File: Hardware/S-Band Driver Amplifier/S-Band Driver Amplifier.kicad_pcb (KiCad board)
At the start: 2 copper layers, 31.8 x 25.4 mm, 15 parts, among them J1 Conn_Coaxial, J2 Conn_Coaxial, U1 SKY65162-70LF

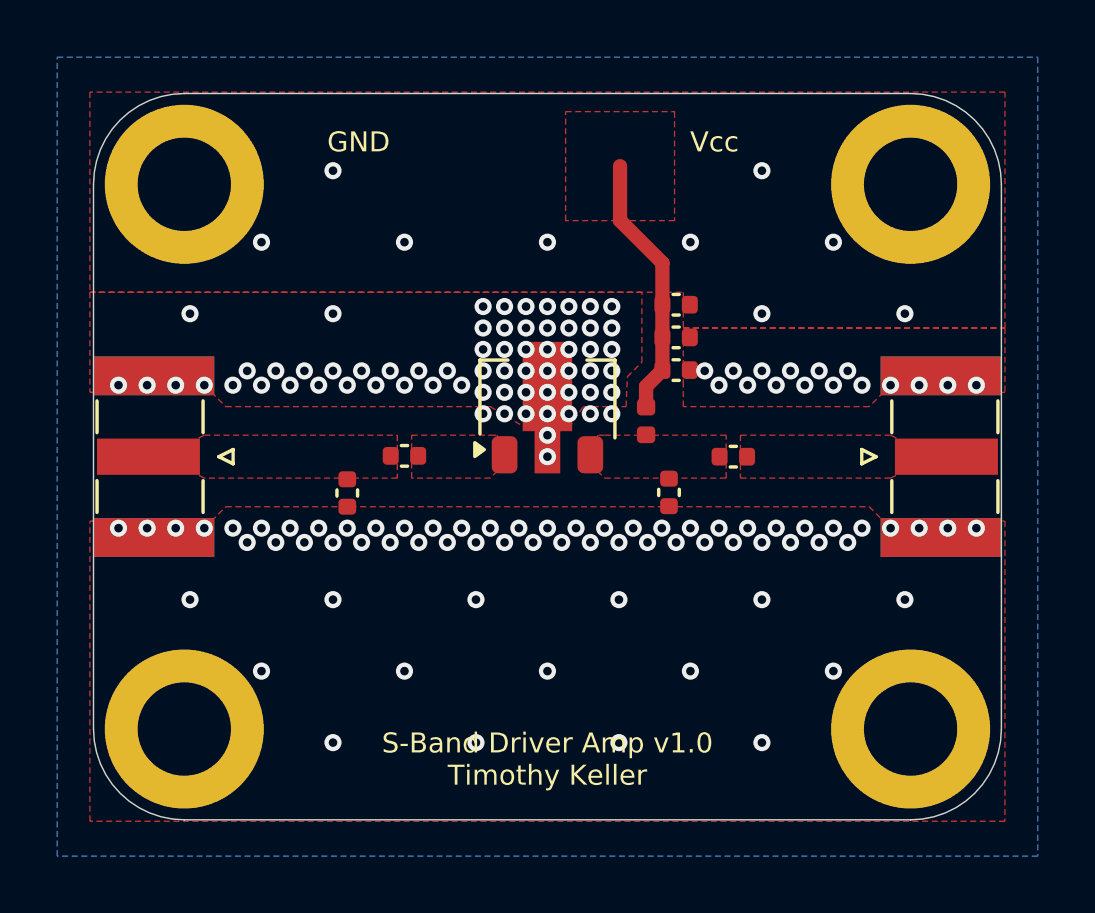
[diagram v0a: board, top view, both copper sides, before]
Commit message: Updating Schematic and Board
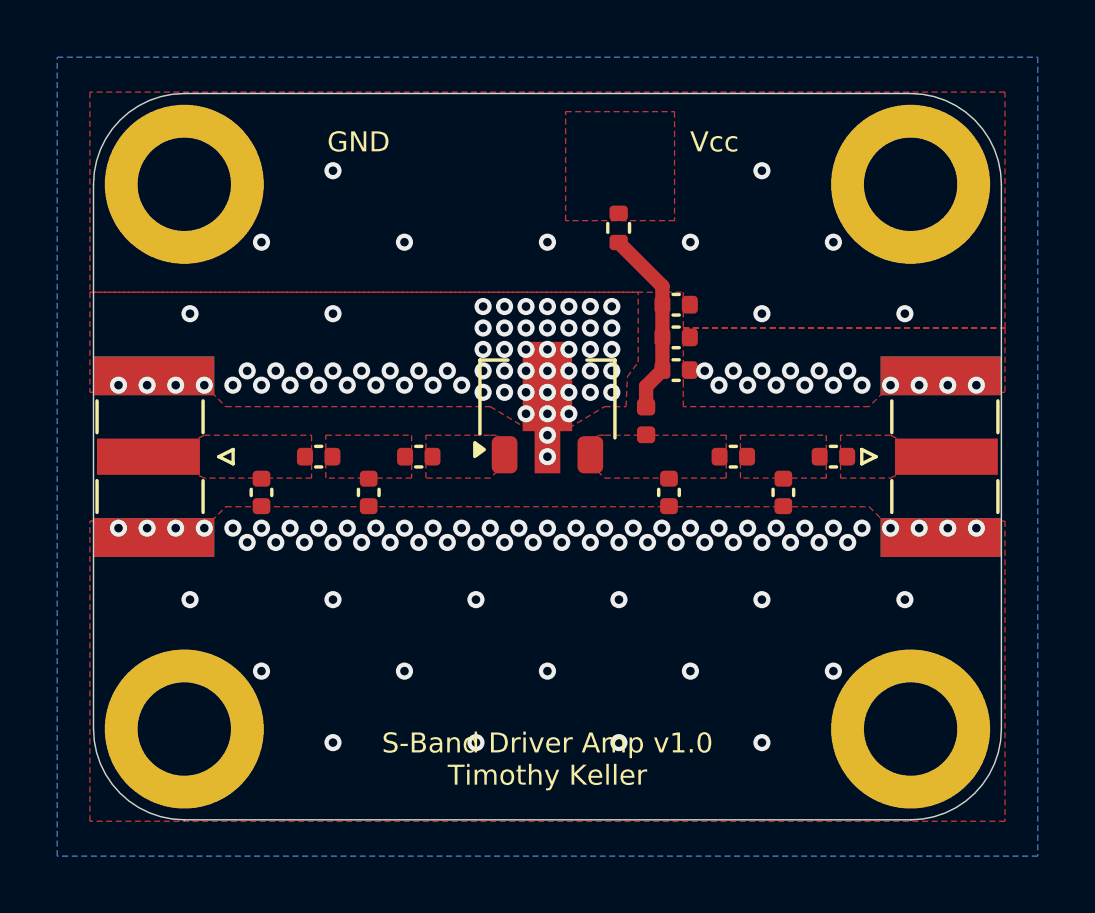
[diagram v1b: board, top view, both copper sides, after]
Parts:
- added C10: 2.7pF, Capacitor_SMD:C_0402_1005Metric, F.Cu at (128.9, 58.4)
- added C11: 4.7pF, Capacitor_SMD:C_0402_1005Metric, F.Cu at (130.7, 57.1)
- added C8: 1.3pF, Capacitor_SMD:C_0402_1005Metric, F.Cu at (116.2, 57.1)
- added C9: 1.3pF, Capacitor_SMD:C_0402_1005Metric, F.Cu at (110.7, 58.4)
- added R1: 0, Resistor_SMD:R_0402_1005Metric, F.Cu at (123.1, 49.1)
- moved C1 3.00 mm to (112.7, 57.1)
- moved C3 0.75 mm to (114.4, 58.4)
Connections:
- net VCC renamed Net-(C5-Pad1)
- C2 pad 2: Net-(J2-In) -> Net-(C10-Pad2)
- C3 pad 2: Net-(J1-In) -> Net-(C1-Pad2)
- U1 pad 1: Net-(C1-Pad2) -> Net-(C8-Pad2)
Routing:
- net Net-(C5-Pad1): track 9.27 -> 6.62 mm
- net GND: vias 160 -> 156
- added copper zone on F.Cu, net Net-(C10-Pad2)
- added copper zone on F.Cu, net Net-(C8-Pad2)
- added copper zone on F.Cu, net VCC
- removed copper zone on F.Cu, net Net-(C5-Pad1)
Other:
- board text added: "0"
- board text added: "1.3pF"
- board text added: "1nF"
- board text added: "1uF"
- board text added: "2.7pF"
- board text added: "4.7pF"
- board text added: "8.7nH"
- board text added: "SKY65162-70LF"
